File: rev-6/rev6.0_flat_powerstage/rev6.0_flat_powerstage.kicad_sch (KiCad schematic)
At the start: 177 parts, among them J1 PHASE_SIG, J2 ENC_SIG, J3 POWER, J4 LED, J5 ANALOG_SIG, J6 VBUS, J7 Motor, Q1 LMG5200, Q2 LMG5200, Q3 LMG5200, U1 AS5047D, U10 LT6350, U11 LP5900SD-3.3/NOPB, U2 INA293B, U3 LT6350, U4 TLV76750DRVR, U5 INA293B, U6 LT6350, U7 LM4040C30FTA, U8 LT6350, U9 INA293B

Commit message: Rev 6 pre design review
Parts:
- removed J1: PHASE_SIG, Connector_PinSocket_2.54mm:PinSocket_1x10_P2.54mm_Horizontal, symbol Connector_Generic:Conn_01x10
- removed J2: ENC_SIG, Connector_PinSocket_2.54mm:PinSocket_1x09_P2.54mm_Horizontal, symbol Connector_Generic:Conn_01x09
- removed J4: LED, Connector_PinSocket_2.54mm:PinSocket_1x04_P2.54mm_Horizontal, symbol Connector_Generic:Conn_01x04
- removed NT2: NetTie_2, NetTie:NetTie-2_SMD_Pad0.5mm, symbol Device:NetTie_2
- removed R15: 2.2k, Resistor_SMD:R_0603_1608Metric, symbol Device:R_Small_US
- removed R16, R32, R48: 15m, project-footprints:KRL3216, symbol Device:R_Shunt_US
- removed R18, R33, R34, R49, R52: 0, Resistor_SMD:R_0603_1608Metric, symbol Device:R_Small_US
- removed R43: 180, Resistor_SMD:R_0603_1608Metric, symbol Device:R_Small_US
- removed R45: 10k, Resistor_SMD:R_0603_1608Metric, symbol Device:R_Small_US
- removed R46, R47: 1k, Resistor_SMD:R_0603_1608Metric, symbol Device:R_Small_US
- removed R56: 499, Resistor_SMD:R_0603_1608Metric, symbol Device:R_Small_US
- removed U2, U5, U9: INA293B, Package_TO_SOT_SMD:SOT-23-5, symbol project:INA293B
- removed U7: LM4040C30FTA, Package_TO_SOT_SMD:SOT-23, symbol Reference_Voltage:LM4040DBZ-3
- added C86, C87: DNP, Capacitor_SMD:C_0402_1005Metric, symbol Device:C_Small
- added C88: 100n, Capacitor_SMD:C_0402_1005Metric, symbol Device:C_Small
- added C89, C90, C91: 3.3n, Capacitor_SMD:C_0805_2012Metric, symbol Device:C_Small
- added C92, C93, C94: 4.7u, Capacitor_SMD:C_0603_1608Metric, symbol Device:C_Small
- added C95, C96: DNP, Capacitor_SMD:C_0603_1608Metric, symbol Device:C_Small
- added FB1, FB2, FB3: BLM31SN500SN1L, Inductor_SMD:L_1206_3216Metric, symbol Device:FerriteBead_Small
- added FL1: 744226S, Inductor_SMD:L_CommonMode_Wuerth_WE-SL2, symbol Device:Filter_EMI_LL_1423
- added J1: PHASE_SIG, Connector_PinSocket_2.54mm:PinSocket_2x07_P2.54mm_Horizontal, symbol Connector_Generic:Conn_02x07_Odd_Even
- added J2: ENC_SIG, Connector_PinSocket_2.54mm:PinSocket_2x06_P2.54mm_Horizontal, symbol Connector_Generic:Conn_02x06_Odd_Even
- added R16: 1k/0.1%, Resistor_SMD:R_0402_1005Metric, symbol Device:R_Small_US
- added R32, R48, R53, R54, R65, R67, R68, R70: 0, Resistor_SMD:R_0402_1005Metric, symbol Device:R_Small_US
- added R34, R61, R69: 10m, project-footprints:R_2512_6332Metric_KELVIN, symbol Device:R_Shunt_US
- added R59, R60: 0, Resistor_SMD:R_1206_3216Metric, symbol Device:R_Small_US
- added R71, R72, R73: 12, Resistor_SMD:R_0805_2012Metric, symbol Device:R_Small_US
- added TP1, TP10, TP11, TP12, TP13, TP14, TP15, TP16, TP17, TP18, TP19, TP2, TP20, TP21, TP22, TP23, TP24, TP25, TP26, TP27, TP28, TP29, TP3, TP30, TP31, TP32, TP33, TP34, TP35, TP36, TP37, TP38, TP39, TP4, TP40, TP41, TP42, TP43, TP44, TP45, TP46, TP47, TP48, TP49, TP5, TP50, TP51, TP52, TP53, TP54, TP55, TP56, TP57, TP58, TP59, TP6, TP60, TP61, TP62, TP63, TP64, TP65, TP7, TP8, TP9: TestPoint_Small, project-footprints:TestPoint_Keystone_5015_Micro-Minature_3DMODEL, symbol Connector:TestPoint_Small
- added U12: LM4040C30FTA, Package_TO_SOT_SMD:SOT-23, symbol Reference_Voltage:LM4040DBZ-3
- added U2, U5, U9: INA240A1PW, Package_SO:TSSOP-8_4.4x3mm_P0.65mm, symbol Amplifier_Current:INA240A1PW
- C1, C13, C17, C2, C20, C24, C25, C28, C29, C3, C31, C35, C37, C39, C4, C41, C43, C47, C48, C49, C5, C51, C56, C58, C6, C60, C62, C66, C67, C69, C7, C71, C72, C73, C74, C75, C78, C8: footprint Capacitor_SMD:C_0603_1608Metric -> Capacitor_SMD:C_0402_1005Metric
- C32: value 4.7u -> DNP; footprint Capacitor_SMD:C_0603_1608Metric -> Capacitor_SMD:C_0402_1005Metric
- C50: value 10u -> DNP
- C59, C82: value 4.7u -> 100n; footprint Capacitor_SMD:C_0603_1608Metric -> Capacitor_SMD:C_0402_1005Metric
- C79: value 4.7u -> DNP
- C80: value 100n -> DNP; footprint Capacitor_SMD:C_0603_1608Metric -> Capacitor_SMD:C_0402_1005Metric
- J3: footprint Connector_PinSocket_2.54mm:PinSocket_1x03_P2.54mm_Horizontal -> Connector_PinSocket_2.54mm:PinSocket_1x02_P2.54mm_Horizontal; symbol Connector_Generic:Conn_01x03 -> Connector_Generic:Conn_01x02
- R1, R4, R5, R7, R8, R9: footprint Resistor_SMD:R_0603_1608Metric -> Capacitor_SMD:C_0402_1005Metric
- R10, R11, R12, R14, R21, R22, R23, R24, R25, R26, R28, R35, R36, R38, R39, R41, R44, R50, R51, R57, R58: footprint Resistor_SMD:R_0603_1608Metric -> Resistor_SMD:R_0402_1005Metric
- R17, R29, R40: value 499 -> 1k/0.1%; footprint Resistor_SMD:R_0603_1608Metric -> Resistor_SMD:R_0402_1005Metric
- R19, R30: value 180 -> 1k/0.1%; footprint Resistor_SMD:R_0603_1608Metric -> Resistor_SMD:R_0402_1005Metric
- R20, R31: value 10k -> 1k/0.1%; footprint Resistor_SMD:R_0603_1608Metric -> Resistor_SMD:R_0402_1005Metric
- R3: value 0 -> 2.2k
- R37: value 75 -> 50
- R55: value 10.2k -> 10.2k/0.1%; footprint Resistor_SMD:R_0603_1608Metric -> Resistor_SMD:R_0402_1005Metric
- R6: value 35.7k -> 35.7k/0.1%; footprint Resistor_SMD:R_0603_1608Metric -> Resistor_SMD:R_0402_1005Metric
- gave numbers to parts that had none: 1
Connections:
- net LED_GND is gone; now on an unnamed net: R3.2
- net LED_PWR is gone; now on net GNDA: R2.2
- net +3V0: now also C29.1, C59.1, C74.1, R19.2, R29.2, R31.2, R16.2, TP61.1, TP63.1, U12.1 (K), U2.6 (REF2), U5.6 (REF2), U9.6 (REF2)
- net +3V3A: now also C88.1, C92.1, C93.1, C94.1, TP14.1, TP60.1, TP62.1, U2.5 (V+), U5.5 (V+), U9.5 (V+); no longer C29.1, C32.1, C59.1, C80.1, R20.2, R31.2
- net +5V: now also TP5.1; no longer C50.1
- net ENC_A: now also J2.3 (Pin_3), TP28.1
- net ENC_B: now also J2.4 (Pin_4), TP29.1
- net GND: now also C25.1, C27.1, C48.1, C50.1, C54.2, C73.1, C77.2, C79.2, C84.2, J3.2 (Pin_2), R2.1, C95.2, C96.2, J1.1 (Pin_1), J1.10 (Pin_10), J1.13 (Pin_13), J1.14 (Pin_14), J1.2 (Pin_2), J1.5 (Pin_5), J1.6 (Pin_6), J1.9 (Pin_9), J2.1 (Pin_1), J2.11 (Pin_11), J2.12 (Pin_12), J2.2 (Pin_2), J2.5 (Pin_5), J2.6 (Pin_6), TP15.1, TP30.1, TP31.1, TP32.1, TP33.1, TP34.1, TP44.1, TP55.1, TP56.1, TP57.1, TP58.1, TP59.1, TP64.1, TP65.1; no longer C25.2, C48.2, C50.2, C73.2, J3.1 (Pin_1), J3.3 (Pin_3)
- net PHA: now also FB1.1, R34.4, TP7.1; no longer C27.1, D4.1 (K), J7.1 (Pin_1), Q1.8, R64.1
- net PHAH: now also J1.3 (Pin_3), TP35.1
- net PHAL: now also J1.4 (Pin_4), TP38.1
- net PHA_ISNS: now also C32.1, R21.1, U3.8 (IN+); no longer C35.1, R19.1, R21.2
- net PHA_ISNS+: now also J5.11 (Pin_11), TP47.1; no longer J5.3 (Pin_3)
- net PHA_ISNS-: now also J5.12 (Pin_12), TP42.1; no longer J5.4 (Pin_4)
- net PHB: now also FB2.1, R61.4, TP8.1; no longer C54.1, D5.1 (K), J7.2 (Pin_2), Q2.8, R63.1
- net PHBH: now also J1.7 (Pin_7), TP36.1
- net PHBL: now also J1.8 (Pin_8), TP39.1
- net PHB_ISNS: now also U6.8 (IN+), R53.1; no longer R30.1
- net PHB_ISNS+: now also TP45.1
- net PHB_ISNS-: now also TP41.1
- net PHC: now also FB3.1, R69.4, TP9.1; no longer C77.1, D6.1 (K), J7.3 (Pin_3), Q3.8, R62.1
- net PHCH: now also J1.11 (Pin_11), TP37.1
- net PHCL: now also J1.12 (Pin_12), TP40.1
- net PHC_ISNS: now also U8.8 (IN+), C86.1, R67.1; no longer C84.1
- net PHC_ISNS+: now also J5.3 (Pin_3), TP46.1; no longer J5.11 (Pin_11)
- net PHC_ISNS-: now also J5.4 (Pin_4), TP27.1; no longer J5.12 (Pin_12)
- net PWRGND: now also C27.2, C50.2, D4.2 (A), D5.2 (A), D6.2 (A), Q1.9, Q2.9, Q3.9, FL1.3, R60.2, R71.2, R72.2, R73.2, TP10.1, TP11.1, TP12.1, TP13.1, TP21.1, TP22.1, TP4.1, TP6.1; no longer D3.1 (K), J6.2 (Pin_2)
- net SPI_MISO: now also J2.8 (Pin_8), TP24.1
- net SPI_MOSI: now also J2.7 (Pin_7), TP23.1
- net SPI_SCK: now also J2.10 (Pin_10), TP25.1
- net SPI_nCS: now also J2.9 (Pin_9), TP26.1
- net VBUS: now also J3.1 (Pin_1), FL1.4, R59.2, TP3.1; no longer J3.2 (Pin_2), J6.1 (Pin_1)
- net VBUS_VSNS+: now also TP48.1
- net VBUS_VSNS-: now also TP43.1
- net at C69.1, C71.1, R40.2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: now also R31.1
- net at C23.1, Q1.6 (VCC), R13.1: now also C25.2; no longer C25.1
- net at C45.1, Q2.6 (VCC), R27.1: now also C48.2; no longer C48.1
- net at C4.1, C6.1, U10.2 (VOCM): now also R17.2, R16.1
- net at C49.1, C51.1, U6.2 (VOCM): now also R29.1, R30.2; no longer R29.2
- net at C28.1, C31.1, U3.2 (VOCM): now also R19.1, R20.2; no longer R17.2
- net at C70.1, Q3.6 (VCC), R42.1: now also C73.2; no longer C73.1
- net at R3.1: now also J6.1 (Pin_1), FL1.1, R59.1, TP1.1
- net +1V5 renamed GNDA
- net GNDA: now also C103.2, C104.2, C105.2, C2.2, C28.2, C29.2, C31.2, C32.2, C37.2, C39.2, C4.2, C49.2, C51.2, C54.1, C56.2, C58.2, C59.2, C6.2, C60.2, C62.2, C64.2, C65.2, C68.2, C69.2, C7.2, C71.2, C74.2, C75.2, C77.1, C78.2, C8.2, C82.2, C84.1, C9.2, R20.1, R30.1, R55.2, U10.6 (V-), U10.9 (EP), U11.3 (GND), U11.7 (GND), U3.6 (V-), U3.9 (EP), U6.6 (V-), U6.9 (EP), U8.6 (V-), U8.9 (EP), C86.2, C88.2, C92.2, C93.2, C94.2, C95.1, C96.1, TP16.1, TP17.1, TP18.1, TP19.1, TP20.1, TP49.1, TP50.1, TP51.1, TP52.1, TP53.1, TP54.1, U12.2 (A), U2.1 (GND), U2.4 (GND), U2.7 (REF1), U5.1 (GND), U5.4 (GND), U5.7 (REF1), U9.1 (GND), U9.4 (GND), U9.7 (REF1); no longer C74.1, R29.1
- removed net EP: C103.2, C104.2, C105.2, C2.2, C28.2, C29.2, C31.2, C32.2, C35.2, C37.2, C39.2, C4.2, C49.2, C51.2, C56.2, C58.2, C59.2, C6.2, C60.2, C62.2, C64.2, C65.2, C68.2, C69.2, C7.2, C71.2, C74.2, C75.2, C78.2, C79.2, C8.2, C80.2, C82.2, C84.2, C9.2, R55.2, U10.6 (V-), U10.9 (EP), U11.3 (GND), U11.7 (EP), U3.6 (V-), U3.9 (EP), U6.6 (V-), U6.9 (EP), U8.6 (V-), U8.9 (EP)
- new net: D6.1 (K), Q3.8, R69.1
- new net: D3.1 (K), FL1.2, J6.2 (Pin_2), R60.1, TP2.1
- new net: C89.2, R71.1
- new net: D4.1 (K), Q1.8, R34.1
- new net: C80.1, R54.2, U5.3 (-)
- new net: C87.2, R70.2, U9.2 (+)
- new net: C87.1, R68.2, U9.3 (-)
- new net: R67.2, U9.8
- new net: R21.2, U2.8
- new net: C35.1, R32.2, U2.3 (-)
- new net: C90.2, R72.1
- new net: R53.2, U5.8
- new net: C91.2, R73.1
- new net: C35.2, R48.2, U2.2 (+)
- new net: D5.1 (K), Q2.8, R61.1
- new net: C80.2, R65.2, U5.2 (+)
- new net PHA_FLT: C91.1, FB1.2, J7.1 (Pin_1), R64.1
- new net PHA_SNS+: R34.3, R48.1
- new net PHA_SNS-: R32.1, R34.2
- new net PHB_FLT: C90.1, FB2.2, J7.2 (Pin_2), R63.1
- new net PHB_SNS+: R61.3, R65.1
- new net PHB_SNS-: R54.1, R61.2
- new net PHC_FLT: C89.1, FB3.2, J7.3 (Pin_3), R62.1
- new net PHC_SNS+: R69.3, R70.1
- new net PHC_SNS-: R68.1, R69.2
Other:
- removed sheet LEDs
- note added: "Motor Phases + EMI filter"
- note removed: "Bias to 55mV min"
- note removed: "LEDs (VERY IMPORTANT)"
- note removed: "Motor Phases"
- note removed: "NO SLEEP ALLOWED"
- note removed: "PWR LED"
- note removed: "Yoink some dead-time losses away from the GaNs"
- moved on the sheet: C12, C14, C15, C16, C19, C22, D1, H1, J6, R55, R6

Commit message: Fix DRC issues on power stage
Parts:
- removed TP60, TP65: TestPoint_Small, project-footprints:TestPoint_Keystone_5015_Micro-Minature_3DMODEL, symbol Connector:TestPoint_Small
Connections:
- net GND: now also U1.5 (TST)
- no-connect marks 0 -> 4

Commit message: Added BoM, fixed footprints
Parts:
- R1, R4, R5, R7, R8, R9: footprint Capacitor_SMD:C_0402_1005Metric -> Resistor_SMD:R_0402_1005Metric
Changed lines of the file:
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@@
       (effects (font (size 1.27 1.27)) (justify left))
     )
-    (property "Footprint" "Capacitor_SMD:C_0402_1005Metric" (id 2) (at 59.69 265.43 0)
+    (property "Footprint" "Resistor_SMD:R_0402_1005Metric" (id 2) (at 59.69 265.43 0)
       (effects (font (size 1.27 1.27)) hide)
     )
@@
       (effects (font (size 1.27 1.27)) (justify left))
     )
-    (property "Footprint" "Capacitor_SMD:C_0402_1005Metric" (id 2) (at 35.56 252.73 0)
+    (property "Footprint" "Resistor_SMD:R_0402_1005Metric" (id 2) (at 35.56 252.73 0)
       (effects (font (size 1.27 1.27)) hide)
     )
@@
       (effects (font (size 1.27 1.27)) (justify left))
     )
-    (property "Footprint" "Capacitor_SMD:C_0402_1005Metric" (id 2) (at 72.39 265.43 0)
+    (property "Footprint" "Resistor_SMD:R_0402_1005Metric" (id 2) (at 72.39 265.43 0)
       (effects (font (size 1.27 1.27)) hide)
     )
@@
       (effects (font (size 1.27 1.27)) (justify left))
     )
-    (property "Footprint" "Capacitor_SMD:C_0402_1005Metric" (id 2) (at 66.04 265.43 0)
+    (property "Footprint" "Resistor_SMD:R_0402_1005Metric" (id 2) (at 66.04 265.43 0)
       (effects (font (size 1.27 1.27)) hide)
     )
@@
       (effects (font (size 1.27 1.27)) (justify left))
     )
-    (property "Footprint" "Capacitor_SMD:C_0402_1005Metric" (id 2) (at 35.56 260.35 0)
+    (property "Footprint" "Resistor_SMD:R_0402_1005Metric" (id 2) (at 35.56 260.35 0)
       (effects (font (size 1.27 1.27)) hide)
     )
@@
       (effects (font (size 1.27 1.27)) (justify left))
     )
-    (property "Footprint" "Capacitor_SMD:C_0402_1005Metric" (id 2) (at 35.4997 257.81 0)
+    (property "Footprint" "Resistor_SMD:R_0402_1005Metric" (id 2) (at 35.4997 257.81 0)
       (effects (font (size 1.27 1.27)) hide)
     )
@@
     )
     (path "/d900d107-82d7-4ff0-bdb1-cc1bab73c1be"
-      (reference "R1") (unit 1) (value "0") (footprint "Capacitor_SMD:C_0402_1005Metric")
+      (reference "R1") (unit 1) (value "0") (footprint "Resistor_SMD:R_0402_1005Metric")
     )
     (path "/dfd99656-7637-4c9b-bca2-3cbeb22e4cdb"
@@
     )
     (path "/8f8dab83-dc28-415c-bf80-44d220a887a7"
-      (reference "R4") (unit 1) (value "0") (footprint "Capacitor_SMD:C_0402_1005Metric")
+      (reference "R4") (unit 1) (value "0") (footprint "Resistor_SMD:R_0402_1005Metric")
     )
     (path "/c6e6fc08-437e-46e0-a577-87ff56709a2a"
-      (reference "R5") (unit 1) (value "0") (footprint "Capacitor_SMD:C_0402_1005Metric")
+      (reference "R5") (unit 1) (value "0") (footprint "Resistor_SMD:R_0402_1005Metric")
     )
     (path "/da761919-2740-46b2-b0f4-4c1cc54b0434"
@@
     )
     (path "/4c757b2a-6edb-48aa-8edc-f5aa02fc0eaf"
-      (reference "R7") (unit 1) (value "DNP") (footprint "Capacitor_SMD:C_0402_1005Metric")
+      (reference "R7") (unit 1) (value "DNP") (footprint "Resistor_SMD:R_0402_1005Metric")
     )
     (path "/a78ab6e9-09af-45d6-b589-84696ef3a227"
-      (reference "R8") (unit 1) (value "DNP") (footprint "Capacitor_SMD:C_0402_1005Metric")
+      (reference "R8") (unit 1) (value "DNP") (footprint "Resistor_SMD:R_0402_1005Metric")
     )
     (path "/a5fc56bc-6146-4503-9ea1-387567c79470"
-      (reference "R9") (unit 1) (value "DNP") (footprint "Capacitor_SMD:C_0402_1005Metric")
+      (reference "R9") (unit 1) (value "DNP") (footprint "Resistor_SMD:R_0402_1005Metric")
     )
     (path "/3b6956bf-96e7-47c7-ba48-241f34547ce0"

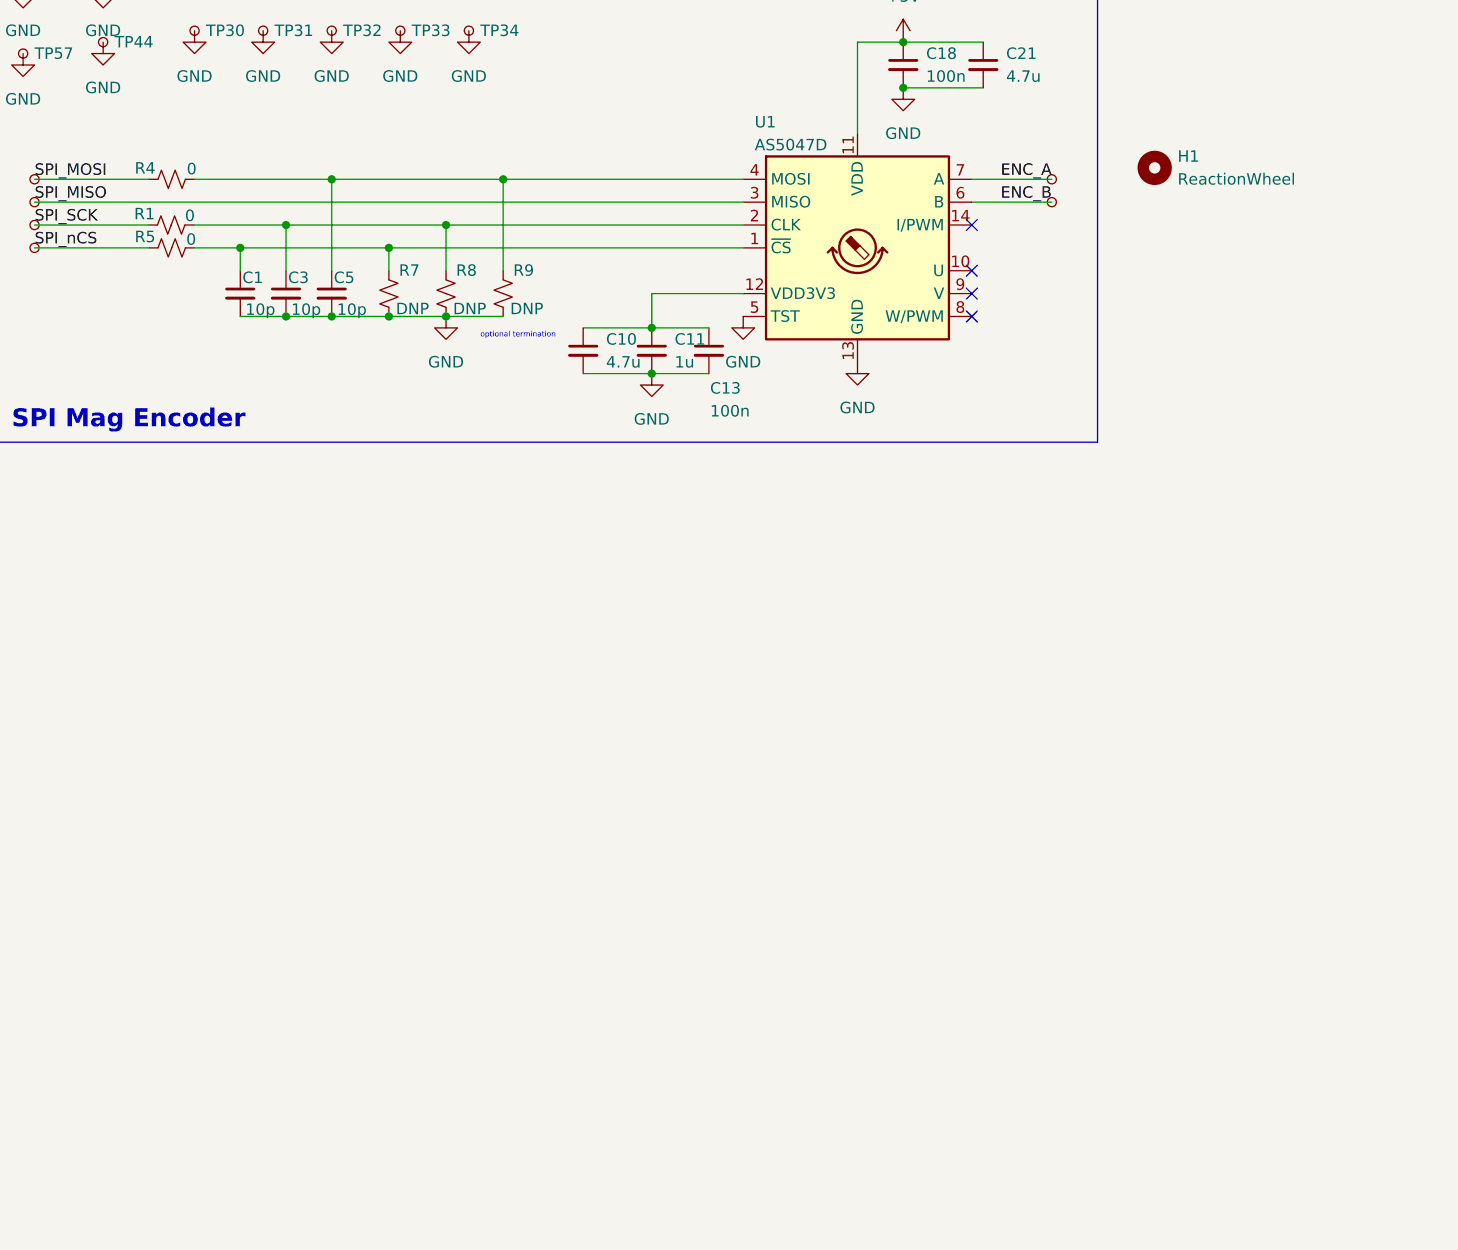
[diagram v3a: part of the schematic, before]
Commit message: Added production files for ground split version
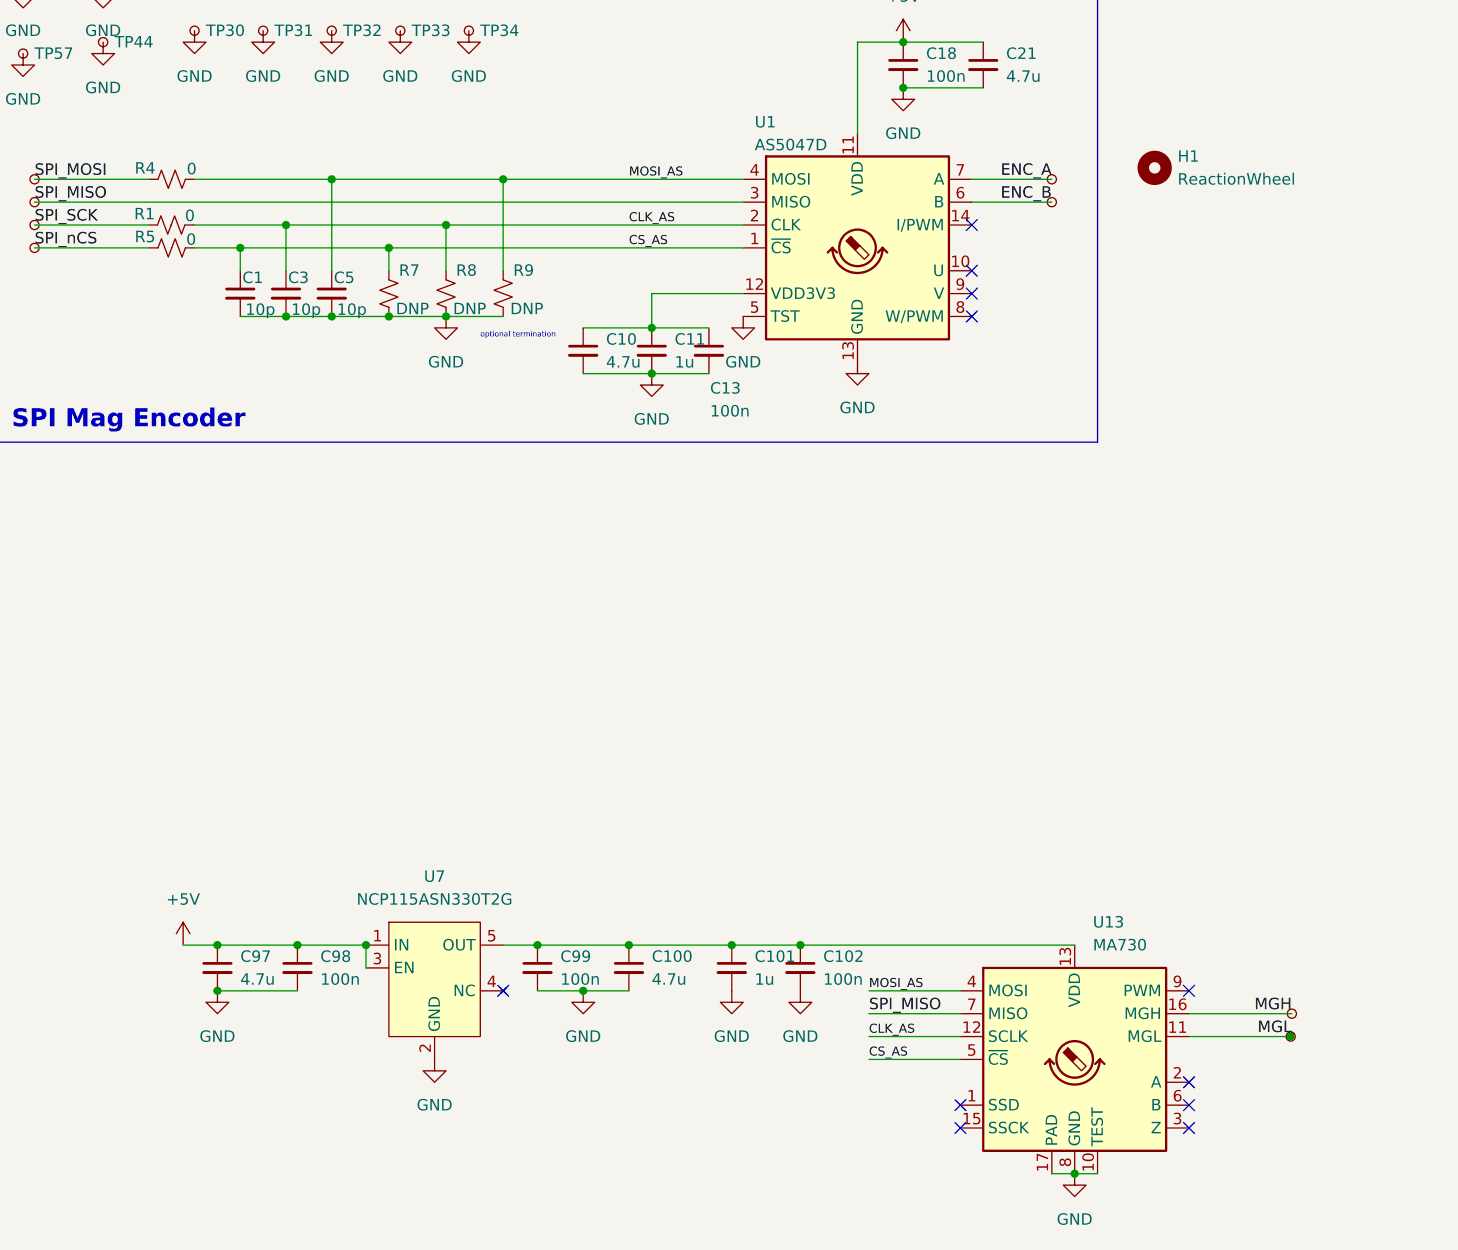
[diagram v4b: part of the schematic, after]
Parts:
- added C100, C97: 4.7u, Capacitor_SMD:C_0402_1005Metric, symbol Device:C_Small
- added C101: 1u, Capacitor_SMD:C_0402_1005Metric, symbol Device:C_Small
- added C102, C98, C99: 100n, Capacitor_SMD:C_0402_1005Metric, symbol Device:C_Small
- added TP60, TP65: TestPoint_Small, TestPoint:TestPoint_Pad_1.0x1.0mm, symbol Connector:TestPoint_Small
- added U13: MA730, Package_DFN_QFN:QFN-16-1EP_3x3mm_P0.5mm_EP1.7x1.7mm, symbol Sensor_Magnetic:MA730
- added U7: NCP115ASN330T2G, Package_TO_SOT_SMD:TSOT-23-5, symbol project:NCP115ASN
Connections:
- net +5V: now also C97.1, C98.1, U7.1 (IN), U7.3 (EN)
- net GND: now also C100.2, C101.2, C102.2, C97.2, C98.2, C99.2, U13.10 (TEST), U13.17 (PAD), U13.8 (GND), U7.2 (GND)
- net SPI_MISO: now also U13.7 (MISO)
- net CLK_AS: now reaches C3.1, R1.2, R8.1, U1.2 (CLK)
- net CLK_AS: now also U13.12 (SCLK)
- net CS_AS: now reaches C1.1, R5.2, R7.1, U1.1 (~{CS})
- net CS_AS: now also U13.5 (~{CS})
- net MOSI_AS: now reaches C5.1, R4.2, R9.1, U1.4 (MOSI)
- net MOSI_AS: now also U13.4 (MOSI)
- new net: C100.1, C101.1, C102.1, C99.1, U13.13 (VDD), U7.5 (OUT)
- new net MGH: TP65.1, U13.16 (MGH)
- new net MGL: TP60.1, U13.11 (MGL)
- no-connect marks 4 -> 11
